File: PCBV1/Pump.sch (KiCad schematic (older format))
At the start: 20 parts, among them J1 Conn_01x02, J5 Conn_01x02, J6 Conn_01x02, J7 Conn_01x02

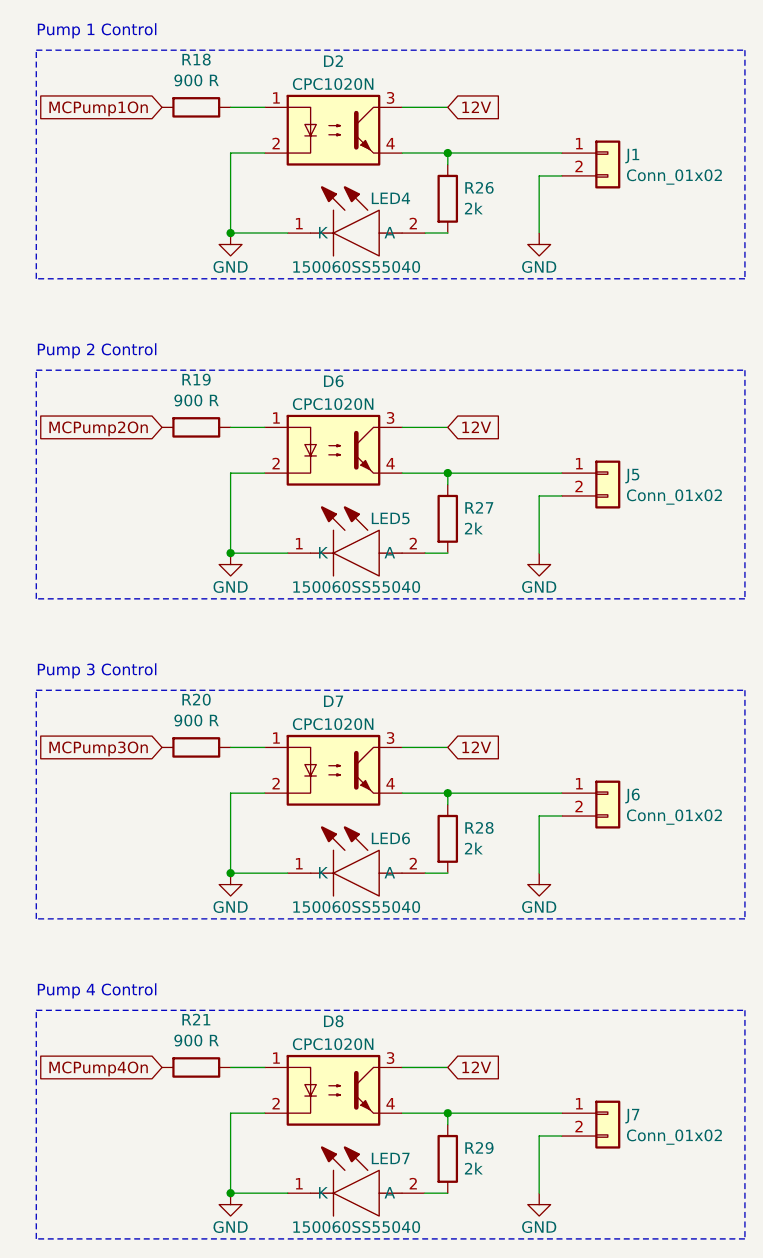
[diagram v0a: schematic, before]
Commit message: Added new JTAG/UART header with connections for STLink V3. Moved from SamacSys to personal GitHub-based library.
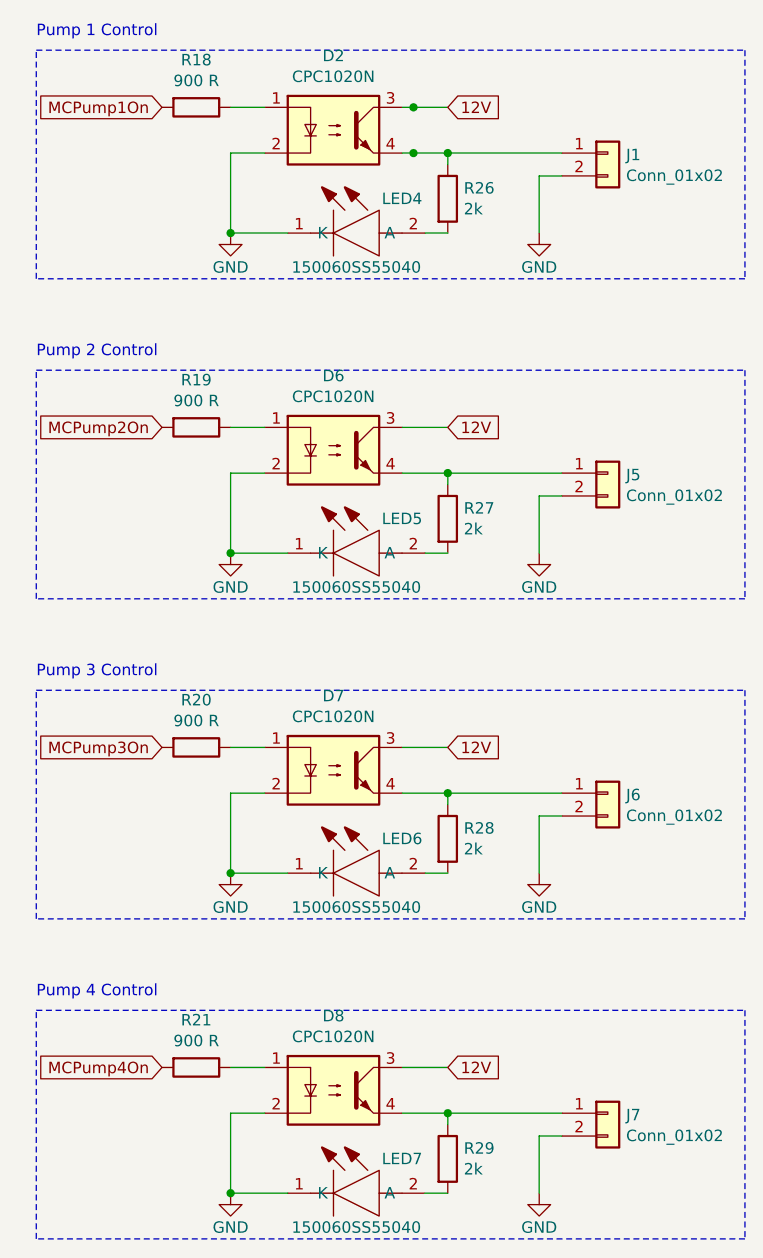
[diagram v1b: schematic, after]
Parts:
- removed D2, D6, D7, D8: CPC1020N, SOP254P610X218-4N, symbol SamacSys_Parts:CPC1020N
- removed LED4, LED5, LED6, LED7: 150060SS55040, 150060SS55040, symbol SamacSys_Parts:150060SS55040
- added D2, D6, D7, D8: CPC1020N, Personal_ICs:CPC1020N, symbol Personal_ICs:CPC1020N
- added LED4, LED5, LED6, LED7: 150060SS55040, Personal_Passives:150060SS55040, symbol Personal_Passives:150060SS55040
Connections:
- net 12V: now also D2.3, D6.3, D7.3, D8.3
- net GND: now also D2.2, D6.2, D7.2, D8.2, LED4.1 (K), LED5.1 (K), LED6.1 (K), LED7.1 (K)
- net at R18.1: now also D2.1
- net at J1.1 (Pin_1), R26.1: now also D2.4
- net at R26.2: now also LED4.2 (A)
- net at R19.1: now also D6.1
- net at J5.1 (Pin_1), R27.1: now also D6.4
- net at R27.2: now also LED5.2 (A)
- net at R20.1: now also D7.1
- net at J6.1 (Pin_1), R28.1: now also D7.4
- net at R28.2: now also LED6.2 (A)
- net at R21.1: now also D8.1
- net at J7.1 (Pin_1), R29.1: now also D8.4
- net at R29.2: now also LED7.2 (A)
